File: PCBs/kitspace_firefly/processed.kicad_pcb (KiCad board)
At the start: 4 copper layers, 85 x 70.5 mm, 80 parts, among them J1 RJ45_Shielded, J101 Conn_02x03_Counter_Clockwise, J102 Analog_1_2, J103 Analog_3_4, J2 RJ45_Shielded, J3 Conn_01x08, J4 Conn_01x08, SW101 SW_DIP_x08, U1 Pico, U103 ADM2687E, U104 AMS1117

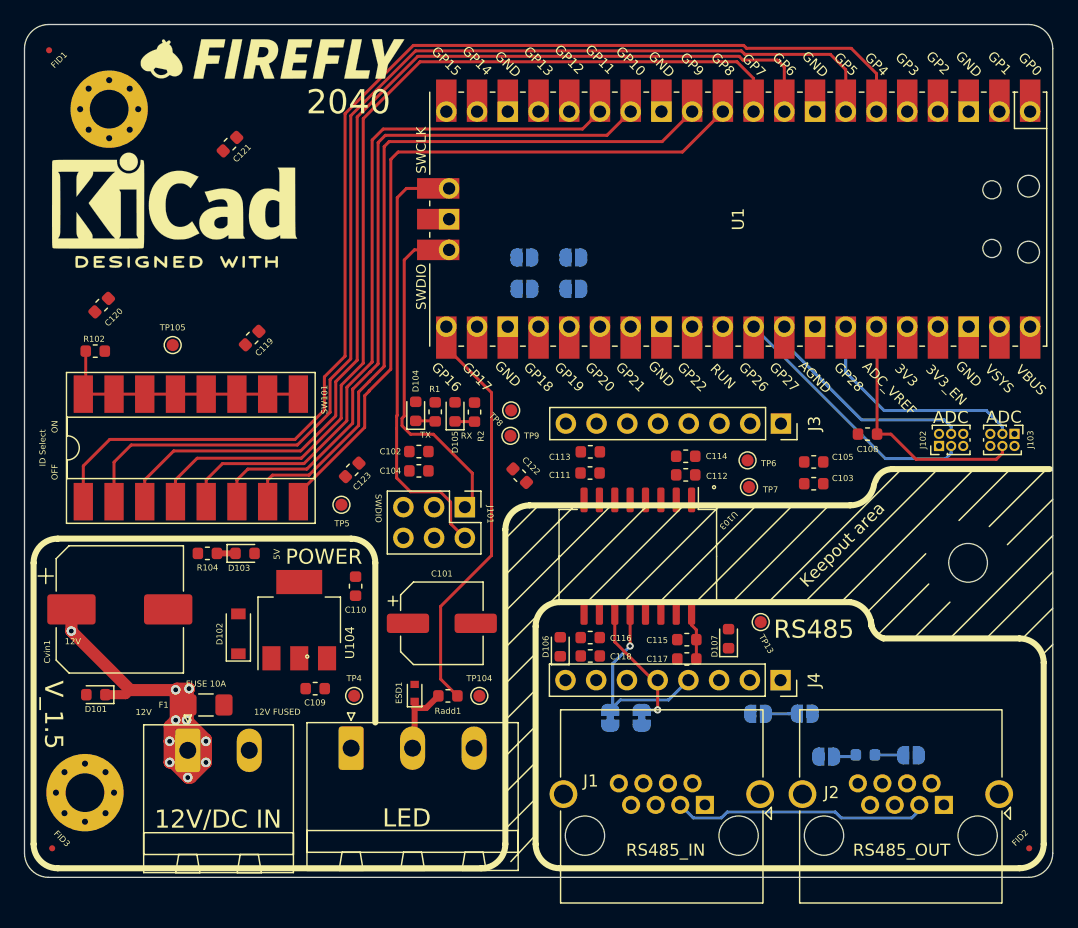
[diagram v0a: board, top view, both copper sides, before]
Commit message: recheck all circuits and clean up fill zone by rerouting the nets using freerouting and manually
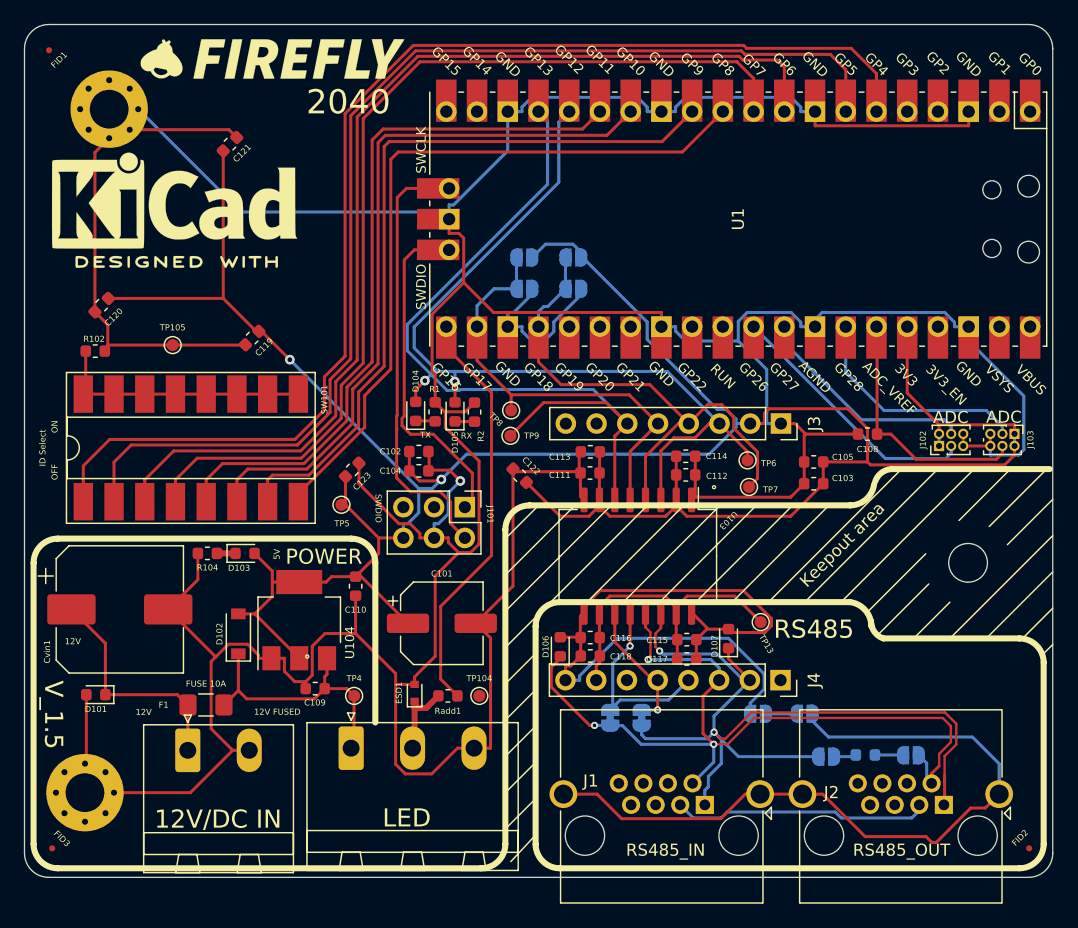
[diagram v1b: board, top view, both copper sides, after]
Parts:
- renumbered G*** to G***_2, G*** to G***_3, REF** to REF**_2
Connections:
- C101 pad 1: (no net) -> +3V3
- C101 pad 2: (no net) -> GND1
- C102 pad 1: (no net) -> +3V3
- C102 pad 2: (no net) -> GND1
- C103 pad 1: (no net) -> +3V3
- C103 pad 2: (no net) -> GND1
- C104 pad 1: (no net) -> +3V3
- C104 pad 2: (no net) -> GND1
- C105 pad 1: (no net) -> +3V3
- C105 pad 2: (no net) -> GND1
- C108 pad 2: (no net) -> GND1
- C109 pad 1: (no net) -> Vin_fused
- C109 pad 2: (no net) -> GND1
- C110 pad 1: (no net) -> +3V3
- C110 pad 2: (no net) -> GND1
- C111 pad 1: (no net) -> +3V3
- C111 pad 2: (no net) -> GND1
- C112 pad 1: (no net) -> GND1
- C112 pad 2: (no net) -> +3V3
- C113 pad 1: (no net) -> GND1
- C113 pad 2: (no net) -> +3V3
- C114 pad 1: (no net) -> +3V3
- C114 pad 2: (no net) -> GND1
- C115 pad 1: (no net) -> DMX_3V
- C116 pad 1: (no net) -> GND2
- C116 pad 2: (no net) -> DMX_3V
- C117 pad 1: (no net) -> DMX_3V
- C118 pad 1: (no net) -> GND2
- C118 pad 2: (no net) -> DMX_3V
- C119 pad 1: (no net) -> +3V3
- C119 pad 2: (no net) -> GND1
- C120 pad 1: (no net) -> +3V3
- C120 pad 2: (no net) -> GND1
- C121 pad 1: (no net) -> +3V3
- C121 pad 2: (no net) -> GND1
- C122 pad 1: (no net) -> +3V3
- C122 pad 2: (no net) -> GND1
- C123 pad 1: (no net) -> +3V3
- C123 pad 2: (no net) -> GND1
- Cvin1 pad 2: (no net) -> GND1
- D101 pad 2: (no net) -> GND1
- D102 pad 1: (no net) -> Vin_fused
- D102 pad 2: (no net) -> +3V3
- D103 pad 2: (no net) -> +3V3
- D104 pad 2: (no net) -> /DMX_Send
- D105 pad 2: (no net) -> /DMX_Receive
- D106 pad 1: (no net) -> /RS485_transciever/DMX-
- D106 pad 2: (no net) -> GND2
- D107 pad 1: (no net) -> /RS485_transciever/DMX+
- D107 pad 2: (no net) -> GND2
- ESD1 pad 2: (no net) -> GND1
- F1 pad 1: (no net) -> Vin_fused
- H1 pad 1: (no net) -> GND1
- H2 pad 1: (no net) -> GND1
- J1 pad 1: (no net) -> /RS485_transciever/DMX+
- J1 pad 2: (no net) -> /RS485_transciever/DMX-
- J1 pad SH: (no net) -> /RS485_transciever/DMXchassignd
- J101 pad 4: (no net) -> GND1
- J101 pad 6: (no net) -> +3V3
- J102 pad 1: (no net) -> +3V3
- J102 pad 2: (no net) -> +3V3
- J102 pad 5: (no net) -> GND1
- J102 pad 6: (no net) -> GND1
- J103 pad 1: (no net) -> +3V3
- J103 pad 2: (no net) -> +3V3
- J103 pad 5: (no net) -> GND1
- J103 pad 6: (no net) -> GND1
- J2 pad 1: (no net) -> /RS485_transciever/DMX+
- J2 pad 2: (no net) -> /RS485_transciever/DMX-
- J2 pad SH: (no net) -> /RS485_transciever/DMXchassignd
- J3 pad 1: (no net) -> GND1
- J3 pad 2: (no net) -> +3V3
- J3 pad 3: (no net) -> /DMX_Receive
- J3 pad 4: (no net) -> /DMX_Enable_Receive
- J3 pad 5: (no net) -> /DMX_Enable_Send
- J3 pad 6: (no net) -> /DMX_Send
- J4 pad 2: (no net) -> /RS485_transciever/DMX+
- J4 pad 3: (no net) -> /RS485_transciever/DMX-
- J4 pad 7: (no net) -> DMX_3V
- J4 pad 8: (no net) -> GND2
- JP1 pad 1: (no net) -> /RS485_transciever/DMX+
- JP101 pad 1: (no net) -> +3V3
- JP101 pad 2: (no net) -> /DMX_Enable_Receive
- JP102 pad 1: (no net) -> /DMX_Enable_Receive
- JP102 pad 2: (no net) -> GND1
- JP103 pad 1: (no net) -> +3V3
- JP103 pad 2: (no net) -> /DMX_Enable_Send
- JP104 pad 1: (no net) -> /DMX_Enable_Send
- JP104 pad 2: (no net) -> GND1
- JP105 pad 2: (no net) -> /RS485_transciever/DMX-
- JP106 pad 2: (no net) -> /RS485_transciever/DMX+
- JP107 pad 1: (no net) -> GND2
- JP108 pad 2: (no net) -> /RS485_transciever/DMXchassignd
- JP2 pad 2: (no net) -> /RS485_transciever/DMX-
- Jadd1 pad 1: (no net) -> Vin_fused
- Jadd1 pad 3: (no net) -> GND1
- Jc1 pad 2: (no net) -> GND1
- R1 pad 1: (no net) -> GND1
- R102 pad 1: (no net) -> GND1
- R104 pad 1: (no net) -> GND1
- R2 pad 1: (no net) -> GND1
- SW101 pad 10: (no net) -> Net-(R102-Pad2)
- SW101 pad 11: (no net) -> Net-(R102-Pad2)
- SW101 pad 12: (no net) -> Net-(R102-Pad2)
- SW101 pad 13: (no net) -> Net-(R102-Pad2)
- SW101 pad 14: (no net) -> Net-(R102-Pad2)
- SW101 pad 15: (no net) -> Net-(R102-Pad2)
- TP105 pad 1: (no net) -> GND1
- TP13 pad 1: (no net) -> DMX_3V
- TP4 pad 1: (no net) -> Vin_fused
- TP5 pad 1: (no net) -> +3V3
- TP6 pad 1: (no net) -> /DMX_Receive
- TP7 pad 1: (no net) -> /DMX_Enable_Receive
- TP8 pad 1: (no net) -> /DMX_Enable_Send
- TP9 pad 1: (no net) -> /DMX_Send
- U1 pad 1: (no net) -> Net-(U1-Pad1)
- U1 pad 13: (no net) -> GND1
- U1 pad 16: (no net) -> /DMX_Receive
- U1 pad 17: (no net) -> /DMX_Send
- U1 pad 18: (no net) -> GND1
- U1 pad 19: (no net) -> Net-(U1-Pad19)
- U1 pad 2: (no net) -> Net-(U1-Pad2)
- U1 pad 20: (no net) -> Net-(U1-Pad20)
- U1 pad 22: (no net) -> /DMX_Enable_Send
- U1 pad 23: (no net) -> GND1
- U1 pad 24: (no net) -> /DMX_Enable_Receive
- U1 pad 25: (no net) -> Net-(U1-Pad25)
- U1 pad 26: (no net) -> Net-(U1-Pad26)
- U1 pad 27: (no net) -> Net-(U1-Pad27)
- U1 pad 28: (no net) -> GND1
- U1 pad 29: (no net) -> Net-(U1-Pad29)
- U1 pad 3: (no net) -> GND1
- U1 pad 30: (no net) -> Net-(U1-Pad30)
- U1 pad 33: (no net) -> GND1
- U1 pad 36: (no net) -> +3V3
- U1 pad 37: (no net) -> Net-(U1-Pad37)
- U1 pad 38: (no net) -> GND1
- U1 pad 39: (no net) -> Net-(U1-Pad39)
- U1 pad 4: (no net) -> Net-(U1-Pad4)
- U1 pad 40: (no net) -> Net-(U1-Pad40)
- U1 pad 42: (no net) -> GND1
- U1 pad 5: (no net) -> Net-(U1-Pad5)
- U1 pad 8: (no net) -> GND1
- U103 pad 1: (no net) -> GND1
- U103 pad 10: (no net) -> DMX_3V
- U103 pad 13: (no net) -> /RS485_transciever/DMX-
- U103 pad 14: (no net) -> /RS485_transciever/DMX+
- U103 pad 15: (no net) -> DMX_3V
- U103 pad 2: (no net) -> +3V3
- U103 pad 3: (no net) -> /DMX_Receive
- U103 pad 4: (no net) -> /DMX_Enable_Receive
- U103 pad 5: (no net) -> /DMX_Enable_Send
- U103 pad 6: (no net) -> /DMX_Send
- U103 pad 7: (no net) -> +3V3
- U103 pad 8: (no net) -> GND1
- U103 pad 9: (no net) -> GND2
- U104 pad 1: (no net) -> GND1
- U104 pad 2: (no net) -> +3V3
- U104 pad 3: (no net) -> Vin_fused
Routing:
- net GND1: track 0.00 -> 458.2 mm, vias 0 -> 1
- net +3V3: track 0.00 -> 235.2 mm, vias 0 -> 2
- net /RS485_transciever/DMX+: track 0.00 -> 73.3 mm, vias 0 -> 2
- net /RS485_transciever/DMX-: track 0.00 -> 69.1 mm, vias 0 -> 3
- net /DMX_Receive: track 0.00 -> 69.1 mm, vias 0 -> 1
- net /DMX_Send: track 0.00 -> 66.7 mm, vias 0 -> 1
- net /RS485_transciever/DMXchassignd: track 0.00 -> 61.0 mm
- net GND2: track 4.01 -> 59.7 mm
- net /DMX_Enable_Receive: track 0.00 -> 44.3 mm
- net /Vin: track 60.6 -> 19.1 mm, vias 10 -> 0
- net /DMX_Enable_Send: track 0.00 -> 36.7 mm
- net DMX_3V: track 0.00 -> 25.9 mm
- net Vin_fused: track 0.00 -> 22.2 mm
